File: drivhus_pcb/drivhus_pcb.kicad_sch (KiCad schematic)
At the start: 102 parts, among them J1 Setup, J10 RS-485 Right Bus, J11 Temp/Humid/Light Indoors, J12 Temp/Humid Outdoors, J13 Pump 1-4, J14 Pump 5-8, J15 Pump 9-12, J16 Pump 13-15, J17 Waterlevel, J18 12V Power connector, J19 Fan, J2 ESP32 Power side, J20 Growlight In, J21 Growlight Out, J22 -12V jumper, J23 +12V jumper, J24 Water valve, J3 ESP32 pin side, J4 RS-485 Left Bus, J5 Conn_Coaxial_Power, J6 +12V, J7 -12V, J8 +5V, J9 -5V, K1 SANYOU_SRD_Form_C, K10 SANYOU_SRD_Form_C, K11 SANYOU_SRD_Form_C, K12 SANYOU_SRD_Form_C, K13 SANYOU_SRD_Form_C, K14 SANYOU_SRD_Form_C, K15 SANYOU_SRD_Form_C, K16 SANYOU_SRD_Form_C, K17 SANYOU_SRD_Form_C, K18 SANYOU_SRD_Form_C, K2 SANYOU_SRD_Form_C, K3 SANYOU_SRD_Form_C, K4 SANYOU_SRD_Form_C, K5 SANYOU_SRD_Form_C, K6 SANYOU_SRD_Form_C, K7 SANYOU_SRD_Form_C, K8 SANYOU_SRD_Form_C, K9 SANYOU_SRD_Form_C, Q1 BC817, Q10 BC817, Q11 BC817, Q12 BC817, Q13 BC817, Q14 BC817, Q15 BC817, Q16 BC817, Q17 BC817, Q18 BC817, Q2 BC817, Q3 BC817, Q4 BC817, Q5 BC817, Q6 BC817, Q7 BC817, Q8 BC817, Q9 BC817, U1 SP3485EN, U2 CD74HC4067M

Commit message: Changed to multiplexed analog sensors and MOSFETs
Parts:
- removed J1: Setup, Connector_PinHeader_2.54mm:PinHeader_1x02_P2.54mm_Vertical, symbol Connector:Conn_01x02_Male
- removed J18: 12V Power connector, TerminalBlock:TerminalBlock_bornier-2_P5.08mm, symbol Connector:Conn_01x02_Male
- removed J19: Fan, TerminalBlock:TerminalBlock_bornier-2_P5.08mm, symbol Connector:Conn_01x02_Male
- removed J2: ESP32 Power side, Connector_PinHeader_2.54mm:PinHeader_1x19_P2.54mm_Vertical, symbol Connector:Conn_01x19_Female
- removed J20: Growlight In, TerminalBlock:TerminalBlock_bornier-2_P5.08mm, symbol Connector:Conn_01x02_Male
- removed J21: Growlight Out, TerminalBlock:TerminalBlock_bornier-2_P5.08mm, symbol Connector:Conn_01x02_Male
- removed J22: -12V jumper, Connector_PinHeader_2.54mm:PinHeader_1x02_P2.54mm_Vertical, symbol Connector:Conn_01x02_Male
- removed J23: +12V jumper, Connector_PinHeader_2.54mm:PinHeader_1x02_P2.54mm_Vertical, symbol Connector:Conn_01x02_Male
- removed J24: Water valve, TerminalBlock:TerminalBlock_bornier-2_P5.08mm, symbol Connector:Conn_01x02_Male
- removed J3: ESP32 pin side, Connector_PinHeader_2.54mm:PinHeader_1x19_P2.54mm_Vertical, symbol Connector:Conn_01x19_Female
- removed J6: +12V, Connector_PinHeader_2.54mm:PinHeader_1x02_P2.54mm_Vertical, symbol Connector:Conn_01x02_Male
- removed J7: -12V, Connector_PinHeader_2.54mm:PinHeader_1x02_P2.54mm_Vertical, symbol Connector:Conn_01x02_Male
- removed J8: +5V, Connector_PinHeader_2.54mm:PinHeader_1x02_P2.54mm_Vertical, symbol Connector:Conn_01x02_Male
- removed J9: -5V, Connector_PinHeader_2.54mm:PinHeader_1x02_P2.54mm_Vertical, symbol Connector:Conn_01x02_Male
- removed K1, K10, K11, K12, K13, K14, K15, K2, K3, K4, K5, K6, K7, K8, K9: SANYOU_SRD_Form_C, Relay_THT:Relay_SPDT_SANYOU_SRD_Series_Form_C, symbol Relay:SANYOU_SRD_Form_C
- removed Q1, Q10, Q11, Q12, Q13, Q14, Q15, Q2, Q3, Q4, Q5, Q6, Q7, Q8, Q9: BC817, Package_TO_SOT_SMD:SOT-23, symbol Transistor_BJT:BC817
- removed U1: SP3485EN, Package_SO:SOIC-8_3.9x4.9mm_P1.27mm, symbol Interface_UART:SP3485EN
- added J1: ESP32 pin side, Connector_PinHeader_2.54mm:PinHeader_1x19_P2.54mm_Vertical, symbol Connector:Conn_01x19_Pin
- added J18: Growlight In, TerminalBlock:TerminalBlock_bornier-2_P5.08mm, symbol Connector:Conn_01x02_Pin
- added J19: -5V, Connector_PinHeader_2.54mm:PinHeader_1x02_P2.54mm_Vertical, symbol Connector:Conn_01x02_Pin
- added J2: Water valve, TerminalBlock:TerminalBlock_bornier-3_P5.08mm, symbol Connector:Conn_01x03_Pin
- added J21: Fan, TerminalBlock:TerminalBlock_bornier-2_P5.08mm, symbol Connector:Conn_01x02_Pin
- added J22: Setup, Connector_PinHeader_2.54mm:PinHeader_1x02_P2.54mm_Vertical, symbol Connector:Conn_01x02_Pin
- added J23: Growlight Out, TerminalBlock:TerminalBlock_bornier-2_P5.08mm, symbol Connector:Conn_01x02_Pin
- added J24: Growlight_-12V/-5V, Connector_PinHeader_2.54mm:PinHeader_1x03_P2.54mm_Vertical, symbol Connector:Conn_01x03_Pin
- added J25: Waterpump_+12V/+5V, Connector_PinHeader_2.54mm:PinHeader_1x03_P2.54mm_Vertical, symbol Connector:Conn_01x03_Pin
- added J26: Fan_-12V/-5V, Connector_PinHeader_2.54mm:PinHeader_1x03_P2.54mm_Vertical, symbol Connector:Conn_01x03_Pin
- added J27: Fan_+12V/+5V, Connector_PinHeader_2.54mm:PinHeader_1x03_P2.54mm_Vertical, symbol Connector:Conn_01x03_Pin
- added J28: Growlight_+12V/+5V, Connector_PinHeader_2.54mm:PinHeader_1x03_P2.54mm_Vertical, symbol Connector:Conn_01x03_Pin
- added J3: ESP32 Power side, Connector_PinHeader_2.54mm:PinHeader_1x19_P2.54mm_Vertical, symbol Connector:Conn_01x19_Pin
- added J33: Sensor 11-15, Connector_RJ:RJ45_Ninigi_GE, symbol Connector:RJ45_Shielded
- added J34: Waterpump_-12V/-5V, Connector_PinHeader_2.54mm:PinHeader_1x03_P2.54mm_Vertical, symbol Connector:Conn_01x03_Pin
- added J6: -12V, Connector_PinHeader_2.54mm:PinHeader_1x02_P2.54mm_Vertical, symbol Connector:Conn_01x02_Pin
- added J7: 12V Power connector, TerminalBlock:TerminalBlock_bornier-2_P5.08mm, symbol Connector:Conn_01x02_Pin
- added J8: +12V, Connector_PinHeader_2.54mm:PinHeader_1x02_P2.54mm_Vertical, symbol Connector:Conn_01x02_Pin
- added J9: +5V, Connector_PinHeader_2.54mm:PinHeader_1x02_P2.54mm_Vertical, symbol Connector:Conn_01x02_Pin
- added Q1: 30N06L-2, Package_TO_SOT_SMD:TO-252-2, symbol Transistor_FET:IPD50R380CE
- added Q10: 30N06L-11, Package_TO_SOT_SMD:TO-252-2, symbol Transistor_FET:IPD50R380CE
- added Q11: 30N06L-12, Package_TO_SOT_SMD:TO-252-2, symbol Transistor_FET:IPD50R380CE
- added Q12: 30N06L-13, Package_TO_SOT_SMD:TO-252-2, symbol Transistor_FET:IPD50R380CE
- added Q13: 30N06L-14, Package_TO_SOT_SMD:TO-252-2, symbol Transistor_FET:IPD50R380CE
- added Q14: 30N06L-15, Package_TO_SOT_SMD:TO-252-2, symbol Transistor_FET:IPD50R380CE
- added Q15: 30N06L-1, Package_TO_SOT_SMD:TO-252-2, symbol Transistor_FET:IPD50R380CE
- added Q2: 30N06L-3, Package_TO_SOT_SMD:TO-252-2, symbol Transistor_FET:IPD50R380CE
- added Q3: 30N06L-4, Package_TO_SOT_SMD:TO-252-2, symbol Transistor_FET:IPD50R380CE
- added Q4: 30N06L-5, Package_TO_SOT_SMD:TO-252-2, symbol Transistor_FET:IPD50R380CE
- added Q5: 30N06L-6, Package_TO_SOT_SMD:TO-252-2, symbol Transistor_FET:IPD50R380CE
- added Q6: 30N06L-7, Package_TO_SOT_SMD:TO-252-2, symbol Transistor_FET:IPD50R380CE
- added Q7: 30N06L-8, Package_TO_SOT_SMD:TO-252-2, symbol Transistor_FET:IPD50R380CE
- added Q8: 30N06L-9, Package_TO_SOT_SMD:TO-252-2, symbol Transistor_FET:IPD50R380CE
- added Q9: 30N06L-10, Package_TO_SOT_SMD:TO-252-2, symbol Transistor_FET:IPD50R380CE
- added R23, R25, R27, R29, R31, R33, R35, R37: 470R, Resistor_SMD:R_1206_3216Metric, symbol Device:R
- added R24, R26, R28, R30, R32, R34, R36: 10K, Resistor_SMD:R_1206_3216Metric, symbol Device:R
- added U1: CD74HC4067M, Package_SO:SOIC-24W_7.5x15.4mm_P1.27mm, symbol 74xx:CD74HC4067M
- J10: value RS-485 Right Bus -> Sensor 6-10
- J4: value RS-485 Left Bus -> Sensor 1-5
- K16: value SANYOU_SRD_Form_C -> Fan_relay
- K17: value SANYOU_SRD_Form_C -> Growlight_relay
- K18: value SANYOU_SRD_Form_C -> Watervalve_relay
- R10, R12, R14, R16, R4, R6, R8: value 1K -> 470R
- R11, R13, R15, R17, R3, R5, R7, R9: value 1K -> 10K
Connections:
- net +12V: now also J2.2 (Pin_2), J25.1 (Pin_1), J27.1 (Pin_1), J28.1 (Pin_1), J7.1 (Pin_1), J8.1 (Pin_1), J8.2 (Pin_2); no longer K16.1
- net +3.3V: now also J3.1 (Pin_1)
- net +5V: now also J10.1, J4.1, J25.3 (Pin_3), J27.3 (Pin_3), J28.3 (Pin_3), J3.19 (Pin_19), J33.1, J9.1 (Pin_1), J9.2 (Pin_2), U1.24 (VCC); no longer D1.1 (K), D10.1 (K), D11.1 (K), D12.1 (K), D13.1 (K), D14.1 (K), D15.1 (K), D2.1 (K), D3.1 (K), D4.1 (K), D5.1 (K), D6.1 (K), D7.1 (K), D8.1 (K), D9.1 (K), J10.5, J4.5
- net -12V: now also J2.1 (Pin_1), J24.1 (Pin_1), J26.1 (Pin_1), J34.1 (Pin_1), J6.1 (Pin_1), J6.2 (Pin_2), J7.2 (Pin_2); no longer J13.1, J13.2, J13.3, J13.6, J13.SH, J14.1, J14.2, J14.3, J14.6, J14.SH, J15.1, J15.2, J15.3, J15.6, J15.SH, J16.1, J16.2, J16.3, J16.6, J16.SH
- net GND: now also J10.2, J10.3, J4.2, J4.3, R11.2, R13.2, R15.2, R17.2, R3.2, R5.2, R7.2, R9.2, J1.1 (Pin_1), J1.7 (Pin_7), J19.1 (Pin_1), J19.2 (Pin_2), J22.2 (Pin_2), J24.3 (Pin_3), J26.3 (Pin_3), J3.14 (Pin_14), J33.2, J33.3, J33.SH, J34.3 (Pin_3), R24.2, R26.2, R28.2, R30.2, R32.2, R34.2, R36.2, U1.12 (GND), U1.15 (~{E}); no longer J10.4, J4.4
- net at K16.3: now also J21.1 (Pin_1)
- net at R14.2: now also Q6.1 (G)
- net -PumpPower: now reaches D12.2 (A)
- net -PumpPower: now also D1.2 (A), D10.2 (A), D11.2 (A), D13.2 (A), D14.2 (A), D15.2 (A), D2.2 (A), D3.2 (A), D4.2 (A), D5.2 (A), D6.2 (A), D7.2 (A), D8.2 (A), D9.2 (A), J34.2 (Pin_2), Q1.3 (S), Q10.3 (S), Q11.3 (S), Q12.3 (S), Q13.3 (S), Q14.3 (S), Q15.3 (S), Q2.3 (S), Q3.3 (S), Q4.3 (S), Q5.3 (S), Q6.3 (S), Q7.3 (S), Q8.3 (S), Q9.3 (S)
- net at J15.8: now also D11.1 (K), Q11.2 (D)
- net at R4.2: now also Q1.1 (G)
- net at J13.8: now also D3.1 (K), Q3.2 (D)
- net at J14.4: now also D4.1 (K), Q4.2 (D)
- net at J14.5: now also D5.1 (K), Q5.2 (D)
- net at J14.7: now also D6.1 (K), Q6.2 (D)
- net at J14.8: now also D7.1 (K), Q7.2 (D)
- net at J15.5: now also D9.1 (K), Q9.2 (D)
- net at J12.7: now also J1.8 (Pin_8)
- net +GrowlightPower: now reaches K17.1
- net +GrowlightPower: now also J18.1 (Pin_1), J28.2 (Pin_2)
- net at R21.1: now also J1.6 (Pin_6)
- net at R4.1, U2.7 (I2): now also R3.1
- net at J15.4: now also D8.1 (K), Q8.2 (D)
- net at J15.7: now also D10.1 (K), Q10.2 (D)
- net at U2.10 (S0): now also J3.10 (Pin_10)
- net at J17.4, R18.2: now also J3.3 (Pin_3)
- net at J17.5, R19.2: now also J3.4 (Pin_4)
- net at R1.2, R2.1: now also J3.5 (Pin_5)
- net at J11.8: now also J3.6 (Pin_6)
- net at U2.1 (COM): now also J3.7 (Pin_7)
- net at U2.11 (S1): now also J3.9 (Pin_9)
- net at U2.4 (I5): now also R10.1, R9.1; no longer R7.1
- net at J16.7: now also D14.1 (K), Q14.2 (D)
- net at R13.1: now also R14.1, U2.2 (I7); no longer U2.20 (I11)
- net at U2.8 (I1): now also R36.1, R37.1; no longer R3.1
- net at U2.23 (I8): now also R15.1, R16.1; no longer R10.1
- net at R10.2: now also Q4.1 (G)
- net at R20.1: now also J1.16 (Pin_16)
- net at R12.2: now also Q5.1 (G)
- net at J11.7: now also J1.2 (Pin_2)
- net at K17.3: now also J23.1 (Pin_1)
- net at R6.2: now also Q2.1 (G)
- net at J10.6: now also U1.23 (I8)
- net at J4.7: now also U1.5 (I4); no longer J10.7
- net at J4.8: now also U1.4 (I5); no longer J10.8
- net at J13.5: now also D2.1 (K), Q1.2 (D)
- net at K18.3: now also J2.3 (Pin_3)
- net at J4.6: now also U1.6 (I3)
- net at U2.13 (S3): now also J1.10 (Pin_10)
- net at R22.1: now also J1.3 (Pin_3)
- net at U2.14 (S2): now also J1.9 (Pin_9)
- net at R11.1: now also R12.1, U2.3 (I6); no longer U2.22 (I9)
- net at R17.1: now also U2.22 (I9), R23.1; no longer U2.16 (I15)
- net at U2.17 (I14): now also R32.1, R33.1; no longer R16.1
- net at U2.18 (I13): now also R30.1, R31.1; no longer R15.1
- net at U2.19 (I12): now also R28.1, R29.1; no longer R14.1
- net at U2.21 (I10): now also R24.1, R25.1; no longer R12.1
- net at R8.1: now also R7.1, U2.5 (I4); no longer U2.3 (I6)
- net at R6.1: now also R5.1, U2.6 (I3); no longer U2.5 (I4)
- net at J13.7: now also D1.1 (K), Q2.2 (D)
- net at J16.4: now also D12.1 (K), Q12.2 (D)
- net at J16.5: now also D13.1 (K), Q13.2 (D)
- net at J13.4: now also D15.1 (K), Q15.2 (D)
- net at R8.2: now also Q3.1 (G)
- net at R16.2: now also Q7.1 (G)
- new net: J3.11 (Pin_11), U1.14 (S2)
- new net: J3.12 (Pin_12), U1.11 (S1)
- new net: J3.13 (Pin_13), U1.1 (COM)
- new net: J3.15 (Pin_15), U1.10 (S0)
- new net: J22.1 (Pin_1), J3.8 (Pin_8)
- new net: Q11.1 (G), R29.2
- new net: Q9.1 (G), R25.2
- new net: Q8.1 (G), R23.2
- new net: R34.1, R35.1, U2.16 (I15)
- new net: Q12.1 (G), R31.2
- new net: Q13.1 (G), R33.2
- new net: R26.1, R27.1, U2.20 (I11)
- new net: Q15.1 (G), R37.2
- new net: Q14.1 (G), R35.2
- new net: J33.4, U1.20 (I11)
- new net: J33.5, U1.19 (I12)
- new net: J33.6, U1.18 (I13)
- new net: J33.7, U1.17 (I14)
- new net: J33.8, U1.16 (I15)
- new net: Q10.1 (G), R27.2
- new net: J4.4, U1.8 (I1)
- new net: J4.5, U1.7 (I2)
- new net: J1.15 (Pin_15), U1.13 (S3)
- new net: J10.5, U1.2 (I7)
- new net: J10.8, U1.21 (I10)
- new net: J10.7, U1.22 (I9)
- new net: J10.4, U1.3 (I6)
- new net +FanPower: J27.2 (Pin_2), K16.1
- new net +PumpPower: J13.1, J13.2, J13.3, J13.6, J13.SH, J14.1, J14.2, J14.3, J14.6, J14.SH, J15.1, J15.2, J15.3, J15.6, J15.SH, J16.1, J16.2, J16.3, J16.6, J16.SH, J25.2 (Pin_2)
- new net -FanPower: J21.2 (Pin_2), J26.2 (Pin_2)
- new net -GrowlightPower: J18.2 (Pin_2), J23.2 (Pin_2), J24.2 (Pin_2)
- no-connect marks 58 -> 30
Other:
- moved on the sheet: D2

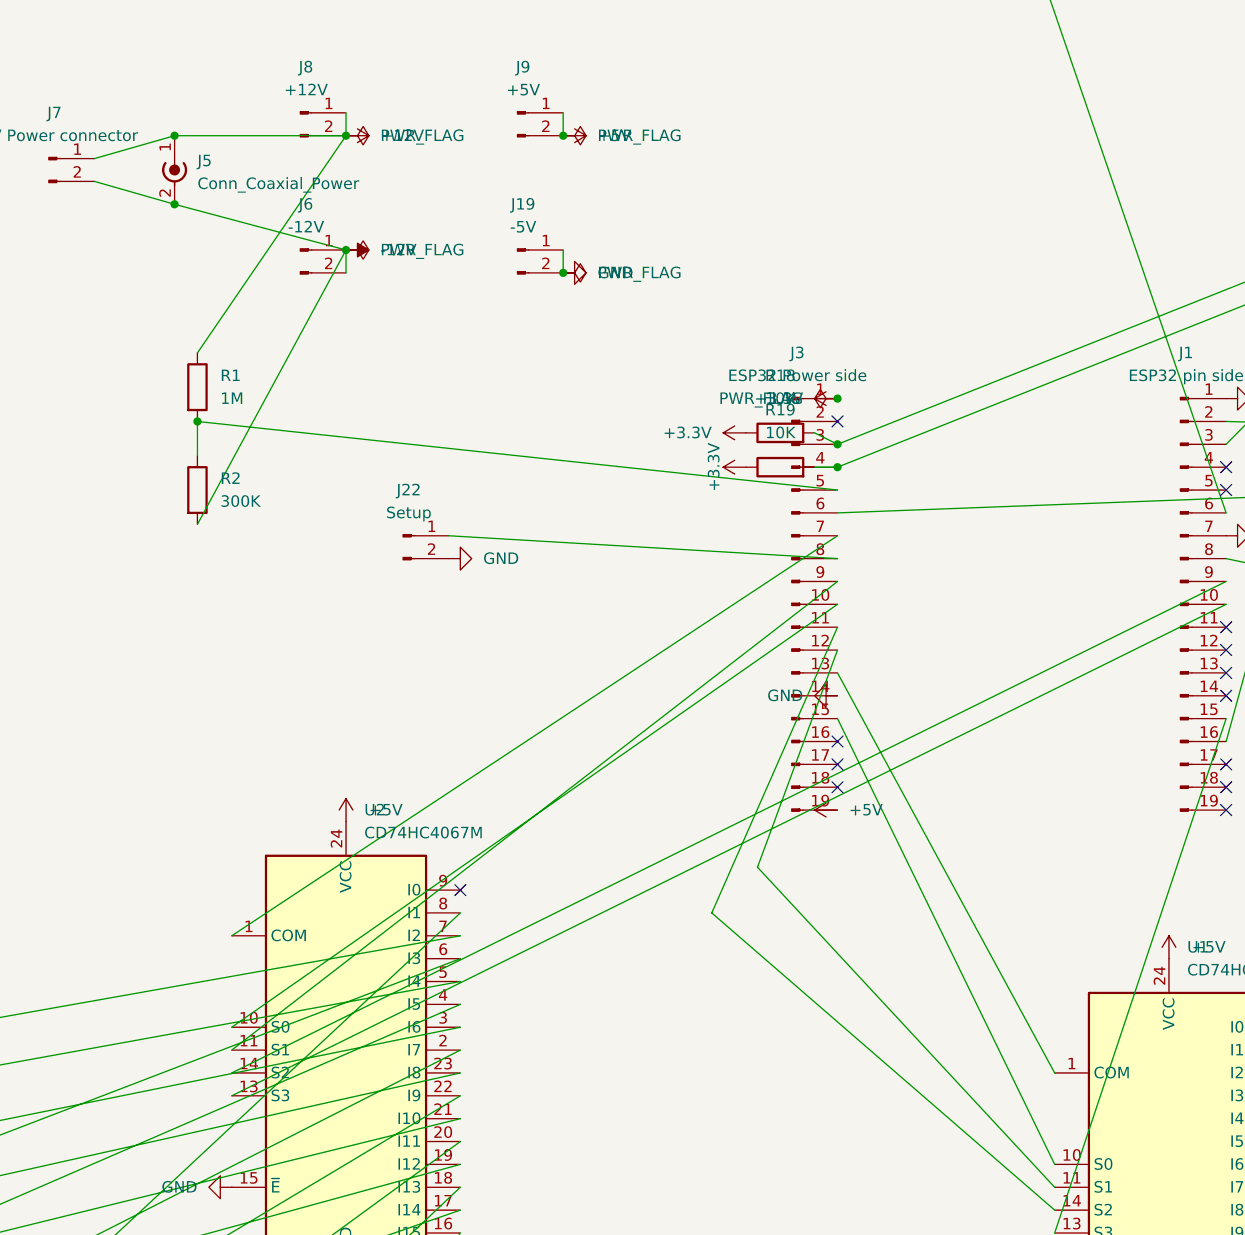
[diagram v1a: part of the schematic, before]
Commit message: Cannot use ADC2 together with WiFi on ESP32
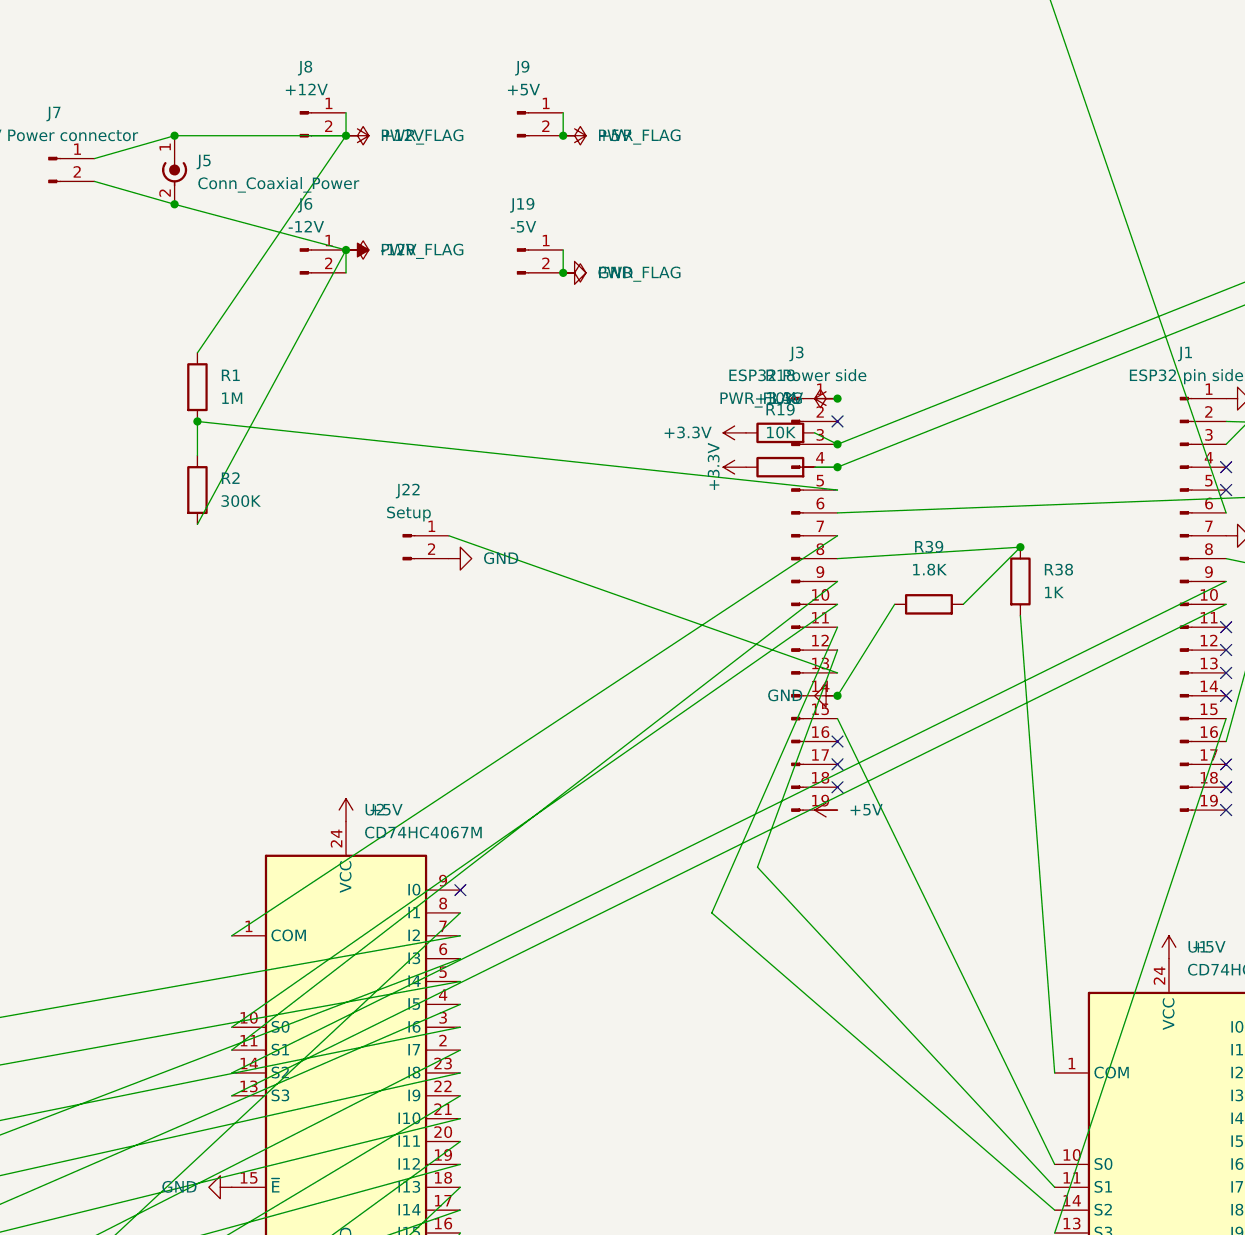
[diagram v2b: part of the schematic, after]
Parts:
- added R38: 1K, Resistor_SMD:R_1206_3216Metric, symbol Device:R
- added R39: 1.8K, Resistor_SMD:R_1206_3216Metric, symbol Device:R
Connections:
- net GND: now also R39.1
- net at J3.13 (Pin_13): now also J22.1 (Pin_1); no longer U1.1 (COM)
- net at J3.8 (Pin_8): now also R38.1, R39.2; no longer J22.1 (Pin_1)
- new net: R38.2, U1.1 (COM)
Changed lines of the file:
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@@
 (kicad_sch
-	(version 20231120)
+	(version 20250114)
 	(generator "eeschema")
-	(generator_version "8.0")
+	(generator_version "9.0")
 	(paper "A1")
 	(junction
@@
 	)
 	(junction
+		(at 622.3 175.26)
+		(diameter 0)
+		(color 0 0 0 0)
+	)
+	(junction
 		(at 373.38 422.91)
 		(diameter 0)
@@
 	)
 	(junction
+		(at 601.98 191.77)
+		(diameter 0)
+		(color 0 0 0 0)
+	)
+	(junction
 		(at 480.06 299.72)
 		(diameter 0)
@@
 	(wire
 		(pts
-			(xy 601.98 189.23) (xy 626.11 233.68)
-		)
-		(stroke
-			(width 0)
-			(type default)
-		)
-	)
-	(wire
-		(pts
 			(xy 152.4 411.48) (xy 139.7 410.21)
 		)
@@
 	(wire
 		(pts
+			(xy 601.98 176.53) (xy 622.3 175.26)
+		)
+		(stroke
+			(width 0)
+			(type default)
+		)
+	)
+	(wire
+		(pts
 			(xy 87.63 375.92) (xy 74.93 407.67)
 		)
@@
 	(wire
 		(pts
+			(xy 626.11 233.68) (xy 622.3 182.88)
+		)
+		(stroke
+			(width 0)
+			(type default)
+		)
+	)
+	(wire
+		(pts
 			(xy 284.48 414.02) (xy 271.78 412.75)
 		)
@@
 	(wire
 		(pts
+			(xy 558.8 173.99) (xy 601.98 189.23)
+		)
+		(stroke
+			(width 0)
+			(type default)
+		)
+	)
+	(wire
+		(pts
 			(xy 731.52 49.53) (xy 735.33 36.83)
 		)
@@
 	(wire
 		(pts
+			(xy 608.33 181.61) (xy 601.98 191.77)
+		)
+		(stroke
+			(width 0)
+			(type default)
+		)
+	)
+	(wire
+		(pts
 			(xy 124.46 415.29) (xy 560.07 226.06)
 		)
@@
 	(wire
 		(pts
+			(xy 622.3 175.26) (xy 615.95 181.61)
+		)
+		(stroke
+			(width 0)
+			(type default)
+		)
+	)
+	(wire
+		(pts
 			(xy 547.37 129.54) (xy 530.86 153.67)
 		)
@@
 	(wire
 		(pts
-			(xy 601.98 186.69) (xy 593.09 210.82)
+			(xy 593.09 210.82) (xy 601.98 186.69)
 		)
 		(stroke
@@
 	(wire
 		(pts
-			(xy 601.98 176.53) (xy 558.8 173.99)
-		)
-		(stroke
-			(width 0)
-			(type default)
-		)
-	)
-	(wire
-		(pts
 			(xy 429.26 355.6) (xy 388.62 417.83)
 		)
@@
 	)
 	(symbol
+		(lib_id "Device:R")
+		(at 612.14 181.61 90)
+		(unit 1)
+		(exclude_from_sim no)
+		(in_bom yes)
+		(on_board yes)
+		(dnp no)
+		(fields_autoplaced yes)
+		(property "Reference" "R39"
+			(at 612.14 175.26 90)
+			(effects
+				(font
+					(size 1.27 1.27)
+				)
+			)
+		)
+		(property "Value" "1.8K"
+			(at 612.14 177.8 90)
+			(effects
+				(font
+					(size 1.27 1.27)
+				)
+			)
+		)
+		(property "Footprint" "Resistor_SMD:R_1206_3216Metric"
+			(at 612.14 183.388 90)
+			(effects
+				(font
+					(size 1.27 1.27)
+				)
+				(hide yes)
+			)
+		)
+		(property "Datasheet" "~"
+			(at 612.14 181.61 0)
+			(effects
+				(font
+					(size 1.27 1.27)
+				)
+				(hide yes)
+			)
+		)
+		(property "Description" "Resistor"
+			(at 612.14 181.61 0)
+			(effects
+				(font
+					(size 1.27 1.27)
+				)
+				(hide yes)
+			)
+		)
+		(pin "2"
+		)
+		(pin "1"
+		)
+		(instances
+			(project ""
+				(path "/5693970b-6852-4141-aaa3-27f18dfba73a"
+					(reference "R39")
+					(unit 1)
+				)
+			)
+		)
+	)
+	(symbol
 		(lib_id "Transistor_FET:IPD50R380CE")
 		(at 299.72 306.07 0)
@@
 	)
 	(symbol
+		(lib_id "Device:R")
+		(at 622.3 179.07 0)
+		(unit 1)
+		(exclude_from_sim no)
+		(in_bom yes)
+		(on_board yes)
+		(dnp no)
+		(fields_autoplaced yes)
+		(property "Reference" "R38"
+			(at 624.84 177.7999 0)
+			(effects
+				(font
+					(size 1.27 1.27)
+				)
+				(justify left)
+			)
+		)
+		(property "Value" "1K"
+			(at 624.84 180.3399 0)
+			(effects
+				(font
+					(size 1.27 1.27)
+				)
+				(justify left)
+			)
+		)
+		(property "Footprint" "Resistor_SMD:R_1206_3216Metric"
+			(at 620.522 179.07 90)
+			(effects
+				(font
+					(size 1.27 1.27)
+				)
+				(hide yes)
+			)
+		)
+		(property "Datasheet" "~"
+			(at 622.3 179.07 0)
+			(effects
+				(font
+					(size 1.27 1.27)
+				)
+				(hide yes)
+			)
+		)
+		(property "Description" "Resistor"
+			(at 622.3 179.07 0)
+			(effects
+				(font
+					(size 1.27 1.27)
+				)
+				(hide yes)
+			)
+		)
+		(pin "2"
+		)
+		(pin "1"
+		)
+		(instances
+			(project ""
+				(path "/5693970b-6852-4141-aaa3-27f18dfba73a"
+					(reference "R38")
+					(unit 1)
+				)
+			)
+		)
+	)
+	(symbol
 		(lib_id "power:PWR_FLAG")
 		(at 560.07 69.85 270)
@@
 		)
 	)
+	(embedded_fonts no)
 )
